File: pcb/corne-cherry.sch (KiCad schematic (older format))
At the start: 96 parts, among them J1 Conn_01x03, J1 MJ-4PP-9, J2 OLED, J3 Conn_01x03, J3 MJ-4PP-9, J4 OLED, SW1 SW_PUSH, SW10 SW_PUSH, SW11 SW_PUSH, SW12 SW_PUSH, SW13 SW_PUSH, SW14 SW_PUSH, SW15 SW_PUSH, SW16 SW_PUSH, SW17 SW_PUSH, SW18 SW_PUSH, SW19 SW_PUSH, SW2 SW_PUSH, SW20 SW_PUSH, SW21 SW_PUSH, SW22 SW_PUSH, SW23 SW_PUSH, SW24 SW_PUSH, SW25 SW_PUSH, SW26 SW_PUSH, SW27 SW_PUSH, SW28 SW_PUSH, SW29 SW_PUSH, SW3 SW_PUSH, SW30 SW_PUSH, SW31 SW_PUSH, SW32 SW_PUSH, SW33 SW_PUSH, SW34 SW_PUSH, SW35 SW_PUSH, SW36 SW_PUSH, SW37 SW_PUSH, SW38 SW_PUSH, SW39 SW_PUSH, SW4 SW_PUSH, SW40 SW_PUSH, SW41 SW_PUSH, SW42 SW_PUSH, SW5 SW_PUSH, SW6 SW_PUSH, SW7 SW_PUSH, SW8 SW_PUSH, SW9 SW_PUSH, U1 ProMicro, U2 ProMicro

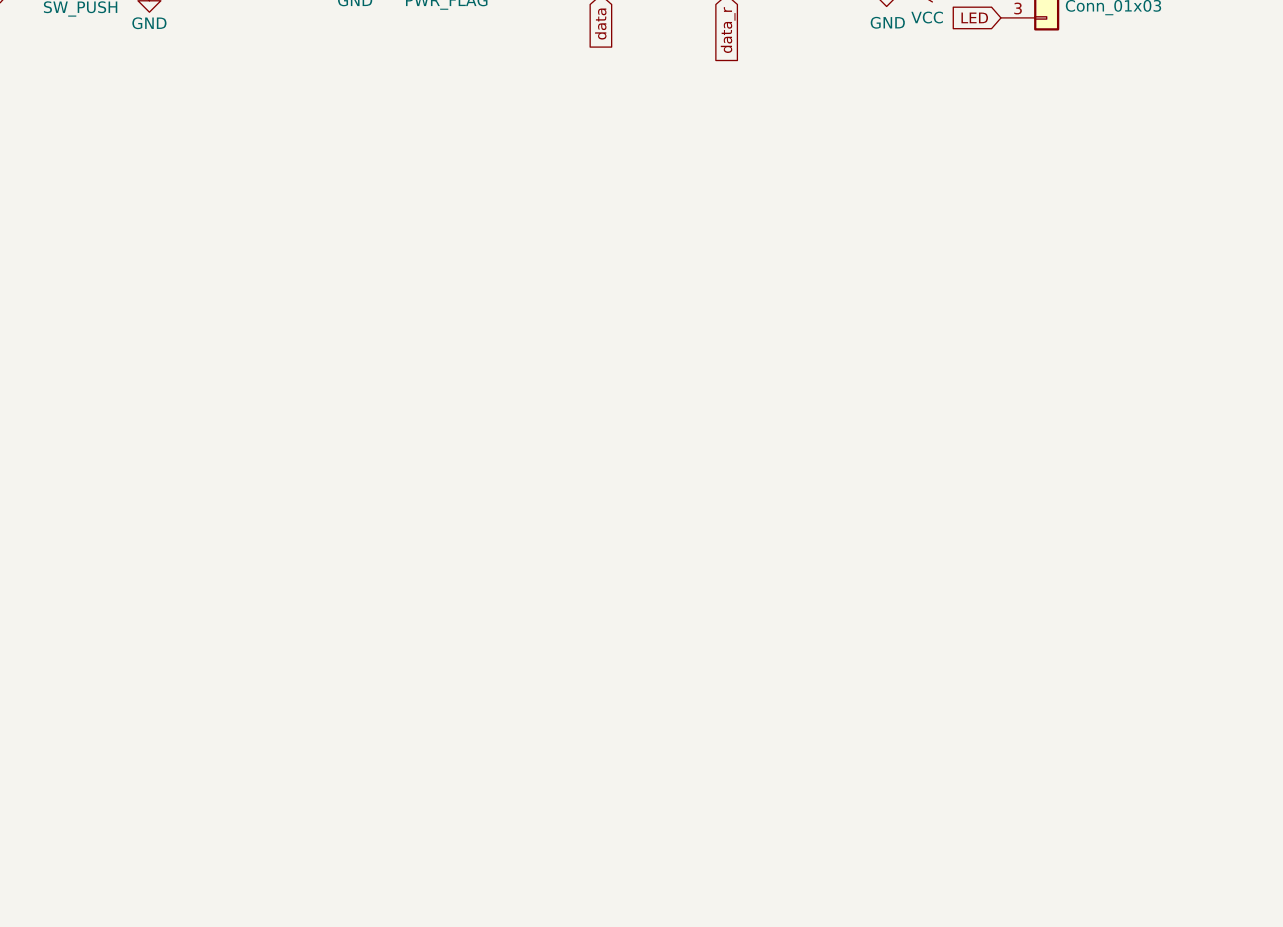
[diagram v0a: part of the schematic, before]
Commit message: Add RGB to left half
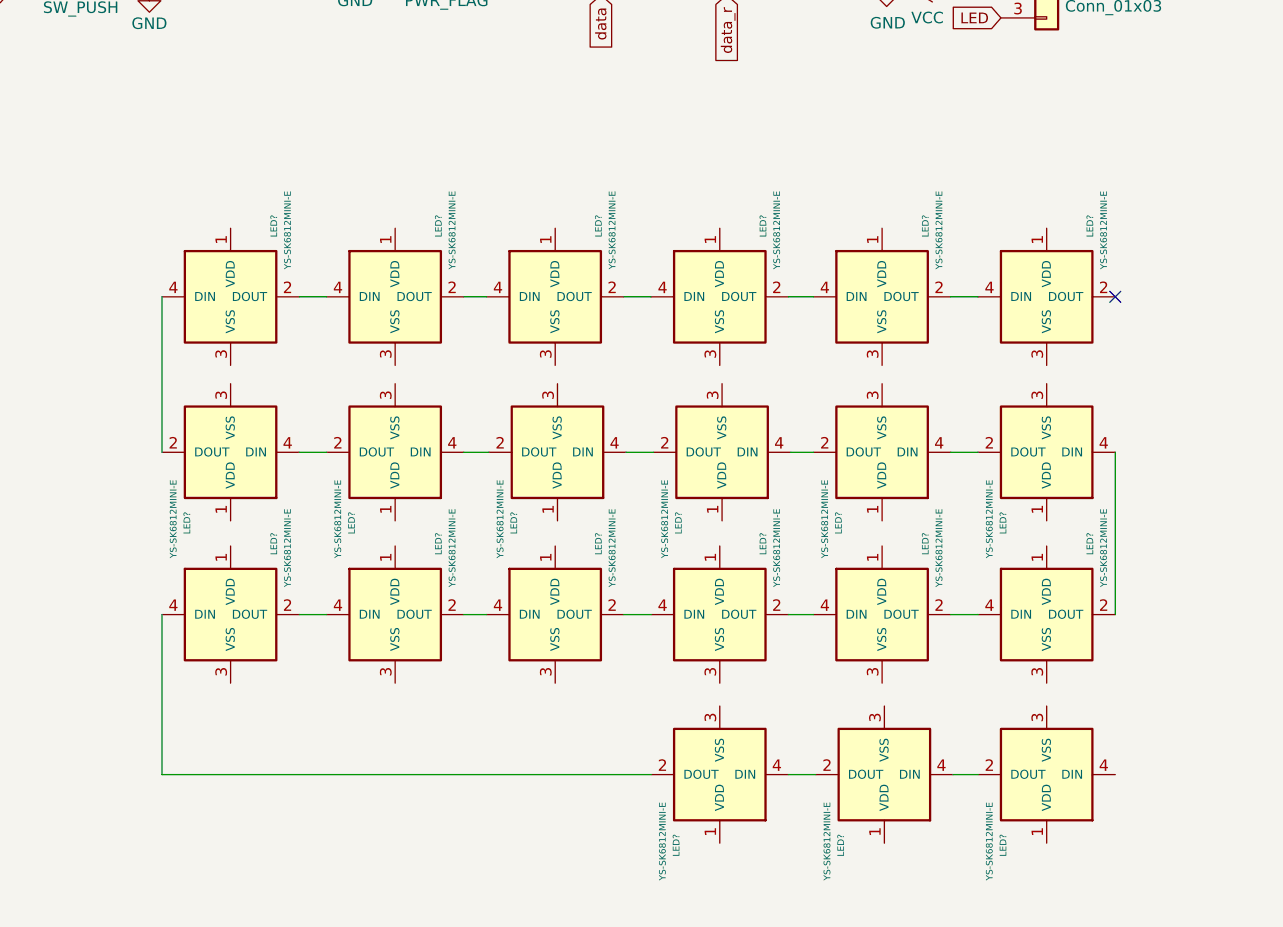
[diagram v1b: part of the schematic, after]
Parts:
- added LED? (x21): YS-SK6812MINI-E, symbol kbd:YS-SK6812MINI-E
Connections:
- new net: LED?.2 (DOUT), LED?.4 (DIN) (x20)
- no-connect marks 12 -> 13

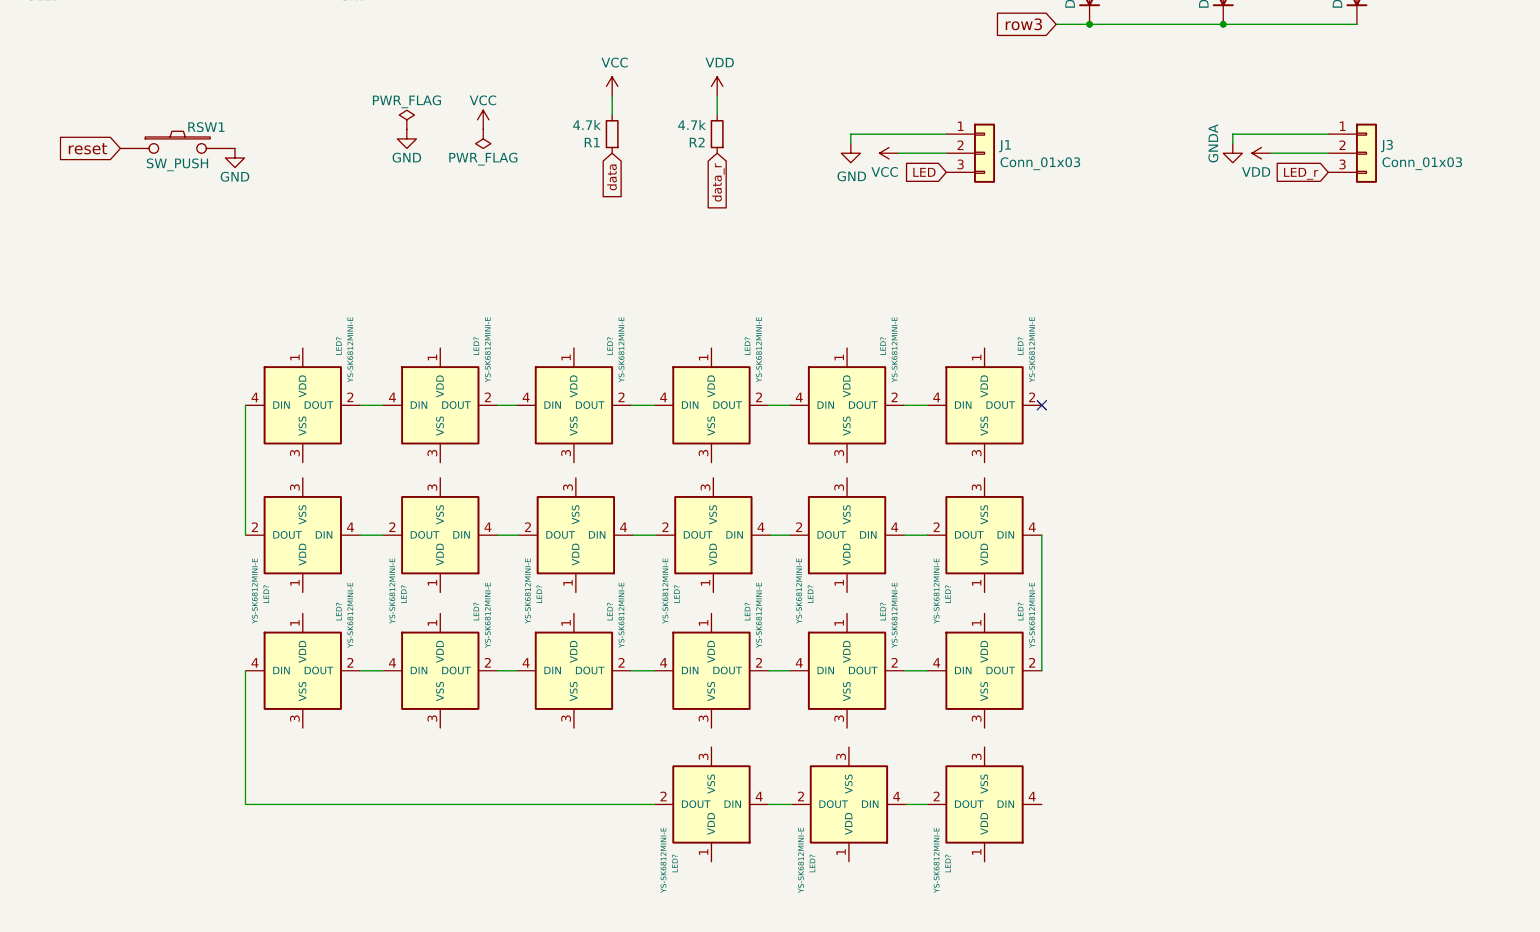
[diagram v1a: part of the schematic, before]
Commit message: Begin RGB placing and routing
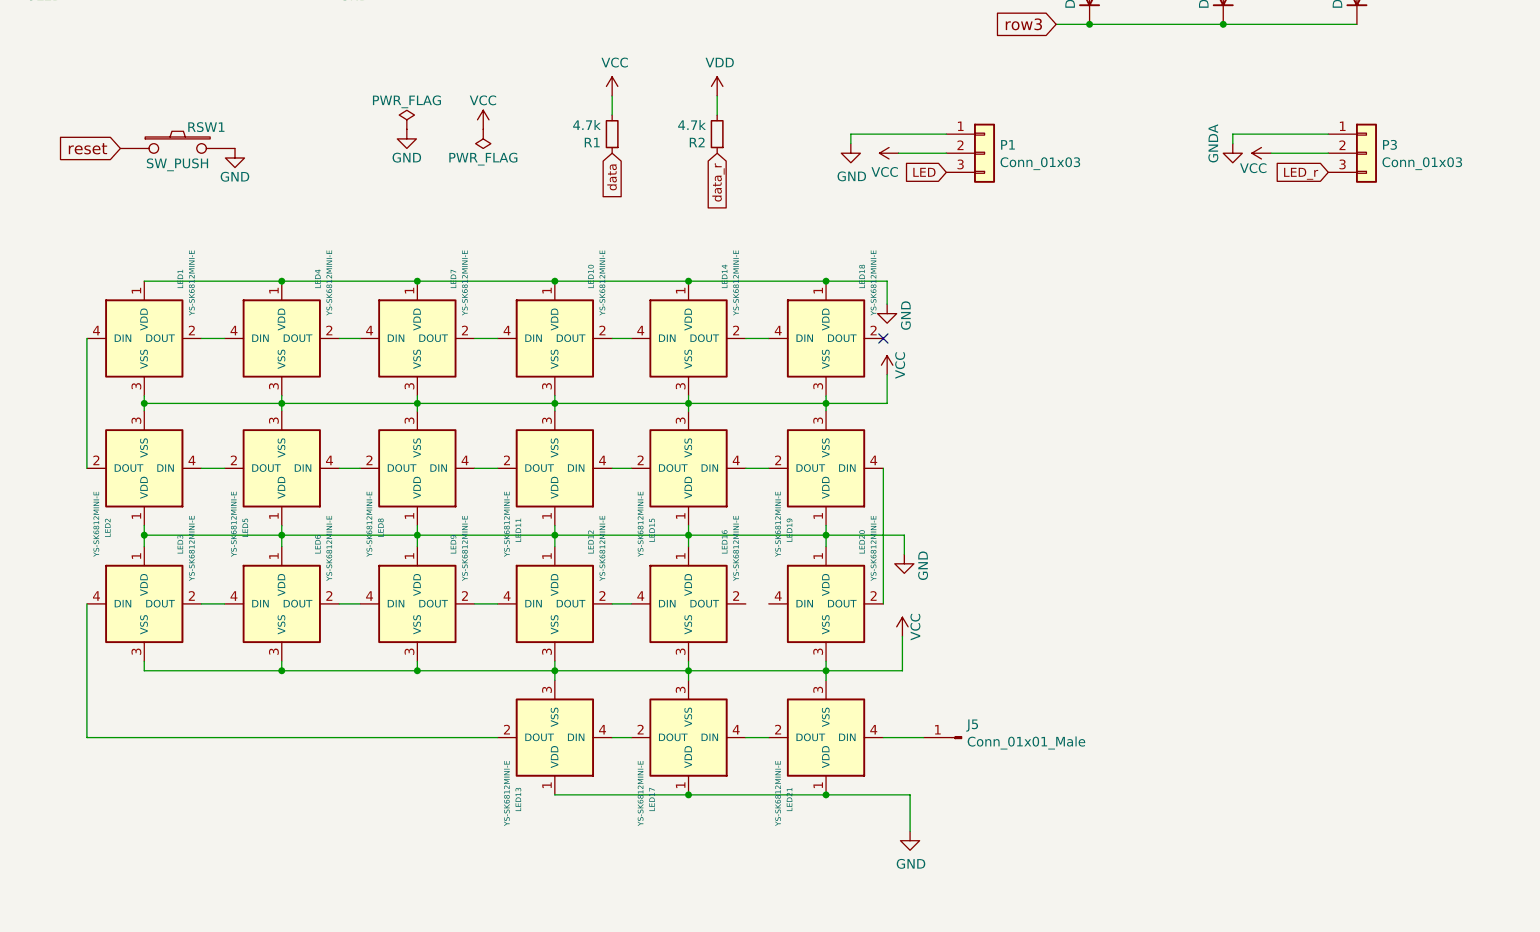
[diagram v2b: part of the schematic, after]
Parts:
- added J5: Conn_01x01_Male, Connector_PinSocket_2.54mm:PinSocket_1x01_P2.54mm_Horizontal, symbol Connector:Conn_01x01_Male
- LED1, LED10, LED11, LED12, LED13, LED14, LED15, LED16, LED17, LED18, LED19, LED2, LED20, LED21, LED3, LED4, LED5, LED6, LED7, LED8, LED9: renamed from LED?; footprint (none) -> kbd:YS-SK6812MINI-E
- renumbered J1 to P1, J3 to P3
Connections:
- net GND: now also LED1.1 (VDD), LED10.1 (VDD), LED11.1 (VDD), LED12.1 (VDD), LED13.1 (VDD), LED14.1 (VDD), LED15.1 (VDD), LED16.1 (VDD), LED17.1 (VDD), LED18.1 (VDD), LED19.1 (VDD), LED2.1 (VDD), LED20.1 (VDD), LED21.1 (VDD), LED3.1 (VDD), LED4.1 (VDD), LED5.1 (VDD), LED6.1 (VDD), LED7.1 (VDD), LED8.1 (VDD), LED9.1 (VDD)
- net VCC: now also LED1.3 (VSS), LED10.3 (VSS), LED11.3 (VSS), LED12.3 (VSS), LED13.3 (VSS), LED14.3 (VSS), LED15.3 (VSS), LED16.3 (VSS), LED17.3 (VSS), LED18.3 (VSS), LED19.3 (VSS), LED2.3 (VSS), LED20.3 (VSS), LED21.3 (VSS), LED3.3 (VSS), LED4.3 (VSS), LED5.3 (VSS), LED6.3 (VSS), LED7.3 (VSS), LED8.3 (VSS), LED9.3 (VSS), P3.2 (Pin_2)
- net VDD: no longer P3.2 (Pin_2)
- net at LED16.2 (DOUT): no longer LED20.4 (DIN)
- net at LED21.4 (DIN): now also J5.1 (Pin_1)
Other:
- moved on the sheet: LED1, LED10, LED11, LED12, LED13, LED14, LED15, LED16, LED17, LED18, LED19, LED2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

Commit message: Finish left half rgb
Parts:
- J5: footprint Connector_PinSocket_2.54mm:PinSocket_1x01_P2.54mm_Horizontal -> Connector_PinHeader_2.54mm:PinHeader_1x01_P2.54mm_Vertical
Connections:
- net VCC: no longer P3.2 (Pin_2)
- net VDD: now also P3.2 (Pin_2)
- net at LED16.2 (DOUT): now also LED20.4 (DIN)
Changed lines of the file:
@@
 F 0 "J5" H 5602 7042 50  0000 R CNN
 F 1 "Conn_01x01_Male" H 5602 7133 50  0000 R CNN
-F 2 "Connector_PinSocket_2.54mm:PinSocket_1x01_P2.54mm_Horizontal" H 5630 7110 50  0001 C CNN
+F 2 "Connector_PinHeader_2.54mm:PinHeader_1x01_P2.54mm_Vertical" H 5630 7110 50  0001 C CNN
 F 3 "~" H 5630 7110 50  0001 C CNN
 	1    5630 7110
@@
 	1    0    0    -1
 $EndComp
-$Comp
-L power:VCC #PWR0105
-U 1 1 60A4DB6E
+Wire Wire Line
+	4620 6410 4500 6410
+$Comp
+L power:VDD #PWR?
+U 1 1 6061D8B6
 P 7250 4050
-F 0 "#PWR0105" H 7250 3900 50  0001 C CNN
-F 1 "VCC" V 7170 4070 50  0000 L CNN
+F 0 "#PWR?" H 7250 3900 50  0001 C CNN
+F 1 "VDD" V 7160 4070 50  0000 L CNN
 F 2 "" H 7250 4050 50  0001 C CNN
 F 3 "" H 7250 4050 50  0001 C CNN

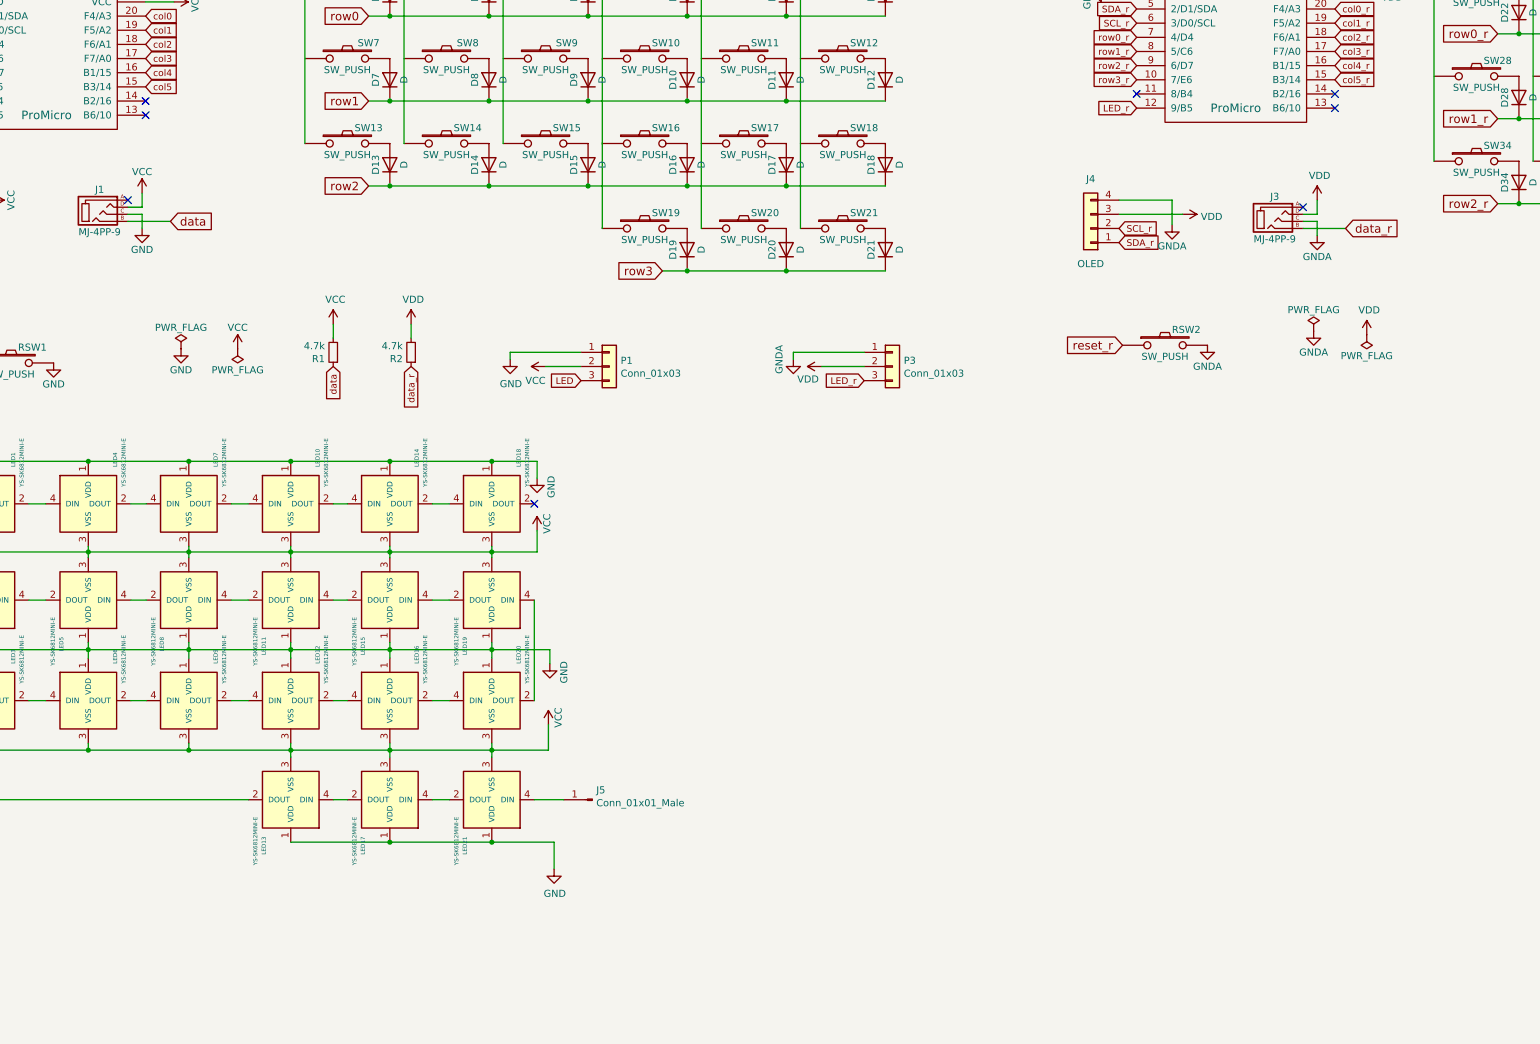
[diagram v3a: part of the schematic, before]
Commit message: Add speakers and RGB on right half
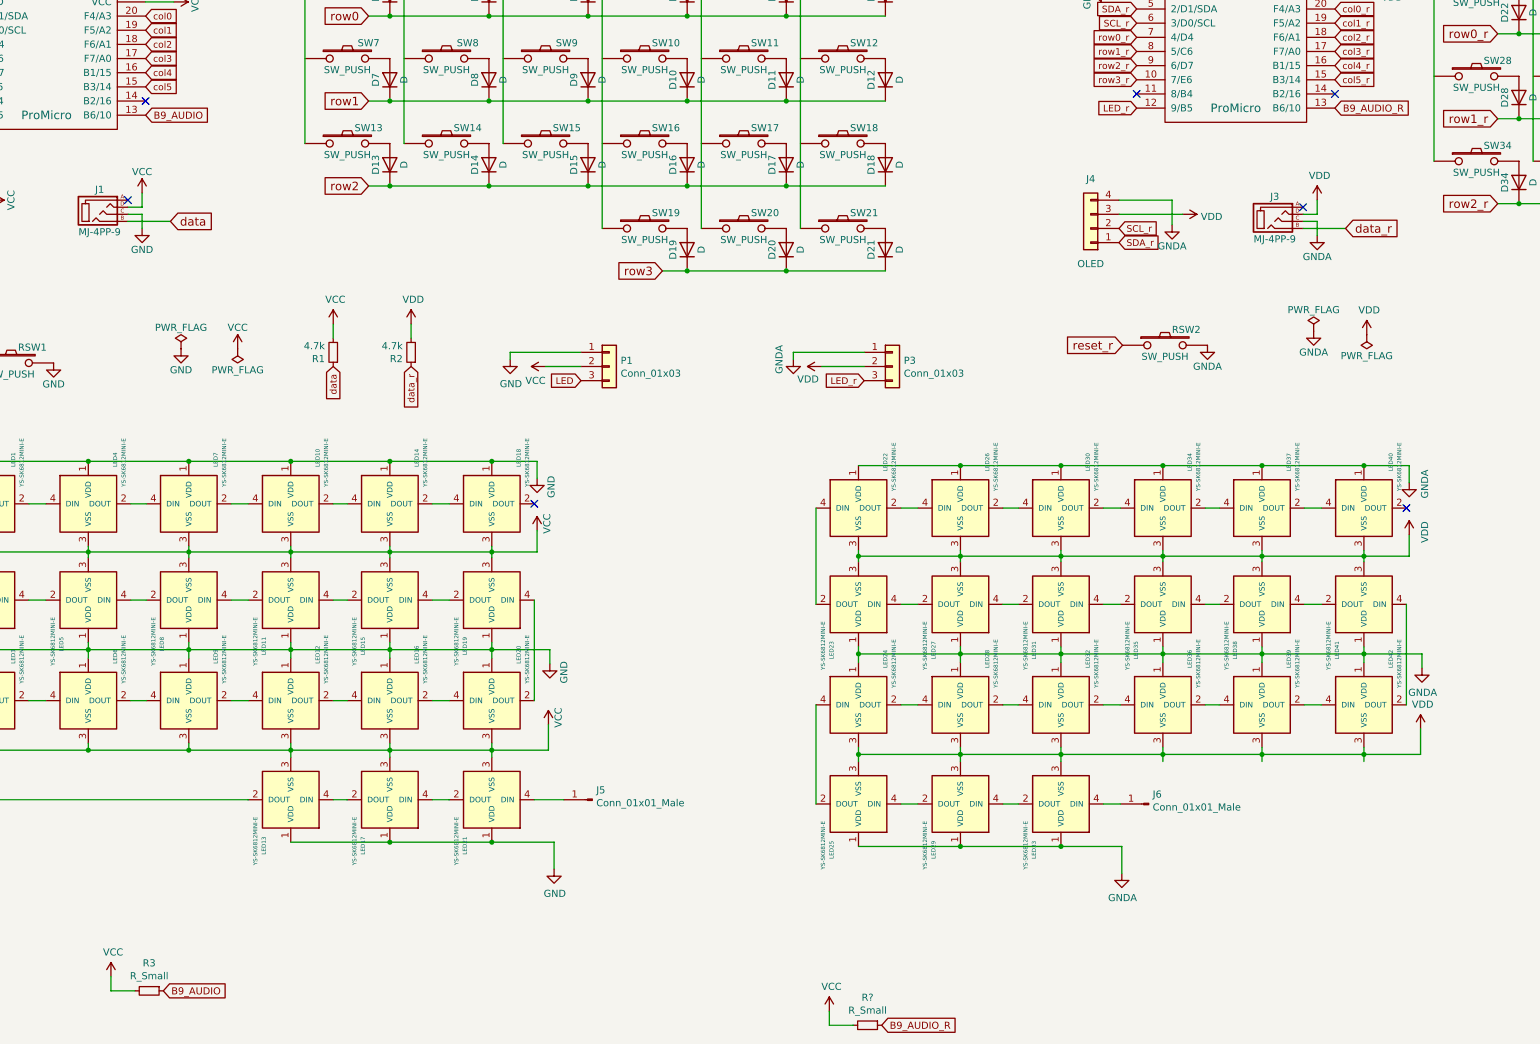
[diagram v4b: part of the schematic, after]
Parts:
- added J6: Conn_01x01_Male, Connector_PinHeader_2.54mm:PinHeader_1x01_P2.54mm_Vertical, symbol Connector:Conn_01x01_Male
- added LED22, LED23, LED24, LED25, LED26, LED27, LED28, LED29, LED30, LED31, LED32, LED33, LED34, LED35, LED36, LED37, LED38, LED39, LED40, LED41, LED42: YS-SK6812MINI-E, kbd:YS-SK6812MINI-E, symbol kbd:YS-SK6812MINI-E
- added R3, R?: R_Small, symbol Device:R_Small
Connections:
- net GNDA: now also LED22.1 (VDD), LED23.1 (VDD), LED24.1 (VDD), LED25.1 (VDD), LED26.1 (VDD), LED27.1 (VDD), LED28.1 (VDD), LED29.1 (VDD), LED30.1 (VDD), LED31.1 (VDD), LED32.1 (VDD), LED33.1 (VDD), LED34.1 (VDD), LED35.1 (VDD), LED36.1 (VDD), LED37.1 (VDD), LED38.1 (VDD), LED39.1 (VDD), LED40.1 (VDD), LED41.1 (VDD), LED42.1 (VDD)
- net VCC: now also R3.2, R?.2
- net VDD: now also LED22.3 (VSS), LED23.3 (VSS), LED24.3 (VSS), LED25.3 (VSS), LED26.3 (VSS), LED27.3 (VSS), LED28.3 (VSS), LED29.3 (VSS), LED30.3 (VSS), LED31.3 (VSS), LED32.3 (VSS), LED33.3 (VSS), LED34.3 (VSS), LED35.3 (VSS), LED36.3 (VSS), LED37.3 (VSS), LED38.3 (VSS), LED39.3 (VSS), LED40.3 (VSS), LED41.3 (VSS), LED42.3 (VSS)
- net B9_AUDIO: now reaches U1.13 (B6/10)
- net B9_AUDIO: now also R3.1
- net B9_AUDIO_R: now reaches U2.13 (B6/10)
- net B9_AUDIO_R: now also R?.1
- new net: LED22.2 (DOUT), LED26.4 (DIN)
- new net: LED22.4 (DIN), LED23.2 (DOUT)
- new net: LED26.2 (DOUT), LED30.4 (DIN)
- new net: LED34.2 (DOUT), LED37.4 (DIN)
- new net: LED30.2 (DOUT), LED34.4 (DIN)
- new net: LED37.2 (DOUT), LED40.4 (DIN)
- new net: LED38.4 (DIN), LED41.2 (DOUT)
- new net: LED41.4 (DIN), LED42.2 (DOUT)
- new net: LED35.4 (DIN), LED38.2 (DOUT)
- new net: LED31.4 (DIN), LED35.2 (DOUT)
- new net: LED27.4 (DIN), LED31.2 (DOUT)
- new net: LED23.4 (DIN), LED27.2 (DOUT)
- new net: LED24.2 (DOUT), LED28.4 (DIN)
- new net: LED24.4 (DIN), LED25.2 (DOUT)
- new net: LED28.2 (DOUT), LED32.4 (DIN)
- new net: LED32.2 (DOUT), LED36.4 (DIN)
- new net: LED39.2 (DOUT), LED42.4 (DIN)
- new net: LED36.2 (DOUT), LED39.4 (DIN)
- new net: LED25.4 (DIN), LED29.2 (DOUT)
- new net: LED29.4 (DIN), LED33.2 (DOUT)
- new net: J6.1 (Pin_1), LED33.4 (DIN)
- no-connect marks 13 -> 12
